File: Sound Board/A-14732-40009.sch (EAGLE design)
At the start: 197 parts, among them P2 AUX IN, P3 AUX OUT, P5 VOLUME, Q1 MPS3646, U1 OKI6295, U12 27C040-150, U13 27C040-150, U14 YAMAHA 2151, U15 TIL7524, U16 74LS374, U17 74LS174, U18 16L8, U19 74LS11, U2 2064, U20 74LS139, U21 74LS14, U22 74LS74, U23 74LS74, U26 74LS04, U28 YAMAHA 3012, U29 LM324D, U3 27C040, U30 MC3340, U31 HA3116, U32 TL084D, U33 TL084D, U4 6809E, U8 74LS138, U9 74LS74, Y1 3.5749MHz, Y2 8MHz

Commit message: 4th sheet added
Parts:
- added IC1: 74LS374DW, 74xx-us:74LS374DW
- added P1: (no value), SparkFun-Connectors:M10X2ROUND_NOSILK
- added P4: ORKIN R/W, SparkFun-Connectors:M04LONGPADS
- added U11, U24, U25: 26LS32A, A-14732-40009:26LS32A
- added U5, U6, U7: 26LS31, A-14732-40009:26LS31
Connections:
- net GND: now also P4.1
- net N$30: now also P4.4
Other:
- moved on the sheet: R4, U16P, U18, U19P, U20P, U21P, U22P, U23P, U26P, U8P, U9P

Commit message: wip
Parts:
- removed IC1: 74LS374DW, 74xx-us:74LS374DW
- added C27, C34, C35, C36, C37, C38, C39, C40, C41, C42, C43: 100pF, SparkFun-Capacitors:1.0UF50V10%(1206)
- added R12, R13, R14, R15, R16, R17, R18, R19, R20, R21, R47, R49, R50, R55, R56, R57, R58: 470, resistor:R-US_R1206
- added U10: 26LS32A, A-14732-40009:26LS32A
- U11, U24: value 26LS32A -> 26LS31; device A-14732-40009:26LS32A -> A-14732-40009:26LS31
- U5: value 26LS31 -> 74LS374DW; device A-14732-40009:26LS31 -> 74xx-us:74LS374DW
- U6: value 26LS31 -> 26LS32A; device A-14732-40009:26LS31 -> A-14732-40009:26LS32A
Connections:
- new net N$104: U5A.2Q, U7.INB
- new net N$105: U5A.3Q, U7.INC
- new net N$106: U5A.4Q, U7.IND
- new net N$107: U11.INA, U5A.5Q
- new net N$108: U11.INB, U5A.6Q
- new net N$109: U11.INC, U5A.7Q
- new net N$110: U11.IND, U5A.8Q
- new net N$111: U11.!EN, U7.!EN
- new net N$112: R58.1, U23B.D, U5A.OC
- new net N$98: U5A.1Q, U7.INA
- net 5V: now also U10.VCC, U11.VCC, U6.VCC, U7.VCC
- net ATE1: now also U23B.CLR, U9B.D, U9B.PRE
- net CPU0: now also U5A.1D, U6.OUTA
- net CPU1: now also U5A.2D, U6.OUTB
- net CPU2: now also U5A.3D, U6.OUTC
- net CPU3: now also U5A.4D, U6.OUTD
- net CPU4: now also U10.OUTA, U5A.5D
- net CPU5: now also U10.OUTB, U5A.6D
- net CPU6: now also U10.OUTC, U5A.7D
- net CPU7: now also U10.OUTD, U5A.8D
- net GND: now also R58.2, U10.EN, U10.GND, U11.EN, U11.GND, U6.GND, U7.EN, U7.GND
- net IRQ: now also U23B.Q
- net RD-LATCH: now also U10.!EN
- net WR-LATCH: now also U5A.CLK, U9B.CLK
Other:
- moved on the sheet: U11, U23B, U24, U6, U7, U9B

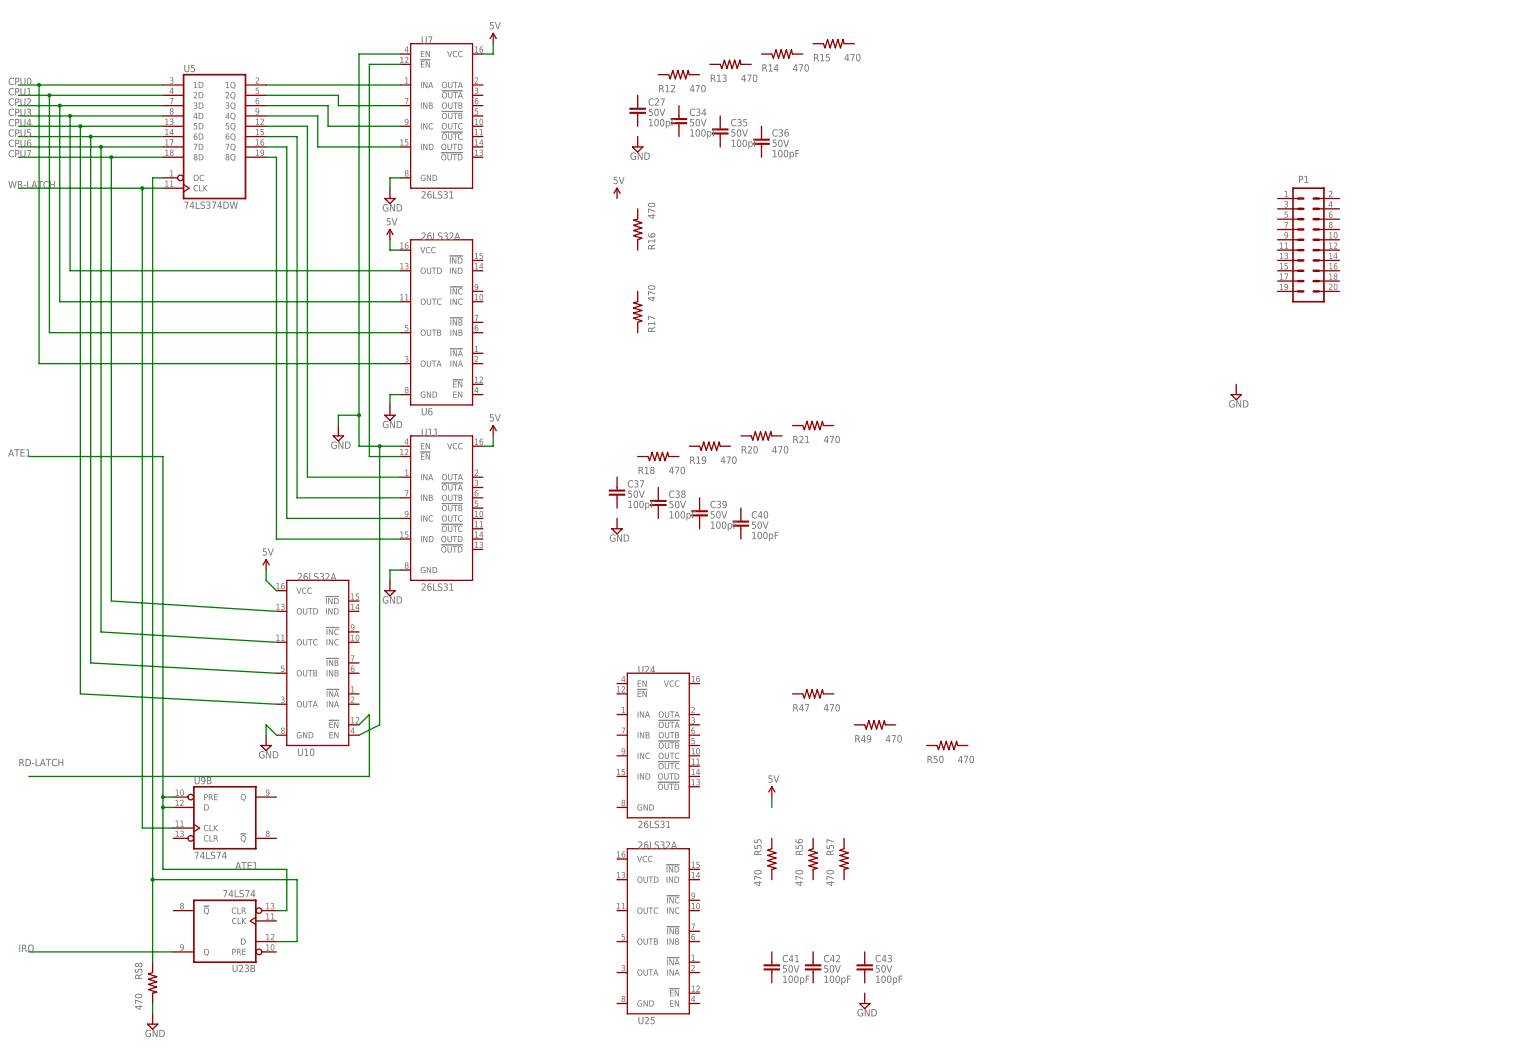
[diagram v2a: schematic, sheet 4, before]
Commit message: almost complete 4th sheet
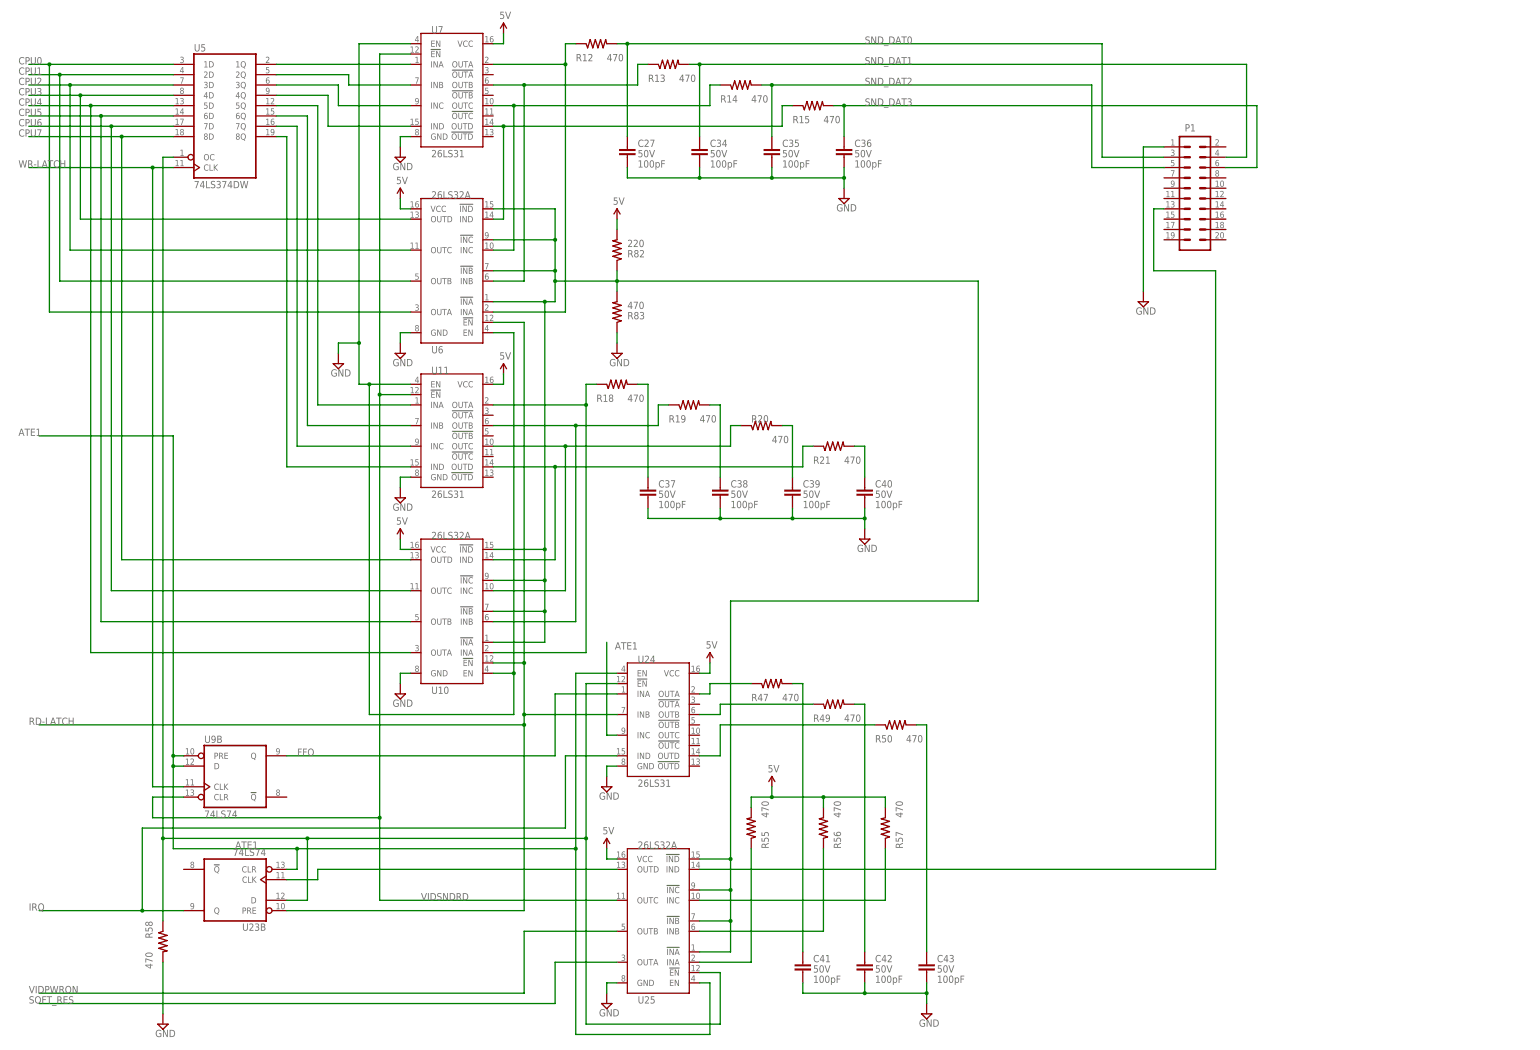
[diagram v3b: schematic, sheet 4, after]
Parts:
- removed R16, R17: 470, resistor:R-US_R1206
- added R82: 220, resistor:R-US_R1206
- added R83: 470, resistor:R-US_R1206
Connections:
- new net FFO: U24.INA, U9B.Q
- new net N$113: U23B.CLK, U25.OUTD
- new net N$114: R58.1, U23B.D, U24.!EN, U25.!EN, U5A.OC
- new net N$115: R12.1, U6.INA, U7.OUTA
- new net N$116: R19.1, U10.INB, U11.OUTB
- new net N$117: R13.1, U6.INB, U7.OUTB
- new net N$118: R20.1, U10.INC, U11.OUTC
- new net N$119: R21.1, U10.IND, U11.OUTD
- new net N$120: R82.1, R83.2, U10.!INA, U10.!INB, U10.!INC, U10.!IND, U25.!INA, U25.!INB, U25.!INC, U25.!IND, U6.!INA, U6.!INB, U6.!INC, U6.!IND
- new net N$121: C37.1, R18.2
- new net N$122: R14.1, U6.INC, U7.OUTC
- new net N$123: R15.1, U6.IND, U7.OUTD
- new net N$124: C38.1, R19.2
- new net N$125: C39.1, R20.2
- new net N$126: C40.1, R21.2
- new net N$127: R49.1, U24.OUTB
- new net N$128: R50.1, U24.OUTD
- new net N$129: C41.1, R47.2
- new net N$130: C42.1, R49.2
- new net N$131: C43.1, R50.2
- new net N$132: R55.1, U25.INA
- new net N$133: R56.1, U25.INB
- new net N$134: R57.1, U25.INC
- new net N$135: P1.13, U25.IND
- new net SND_DAT0: C27.1, P1.3, R12.2
- new net SND_DAT1: C34.1, P1.4, R13.2
- new net SND_DAT2: C35.1, P1.5, R14.2
- new net SND_DAT3: C36.1, P1.6, R15.2
- new net VIDSNDRD: U11.!EN, U25.OUTC, U7.!EN, U9B.CLR
- net 5V: now also R55.2, R56.2, R57.2, R82.2, U24.VCC, U25.VCC
- net ATE1: now also U24.EN, U24.INC, U25.EN
- net GND: now also C27.2, C34.2, C35.2, C36.2, C37.2, C38.2, C39.2, C40.2, C41.2, C42.2, C43.2, P1.1, R83.1, U24.GND, U25.GND, U6.EN
- net IRQ: now also U24.IND
- net N$111: now also R47.1, U24.OUTA; no longer U11.!EN, U7.!EN
- net N$112: now also R18.1, U10.INA, U11.OUTA; no longer R58.1, U23B.D, U5A.OC
- net RD-LATCH: now also U23B.PRE, U24.INB, U6.!EN
- net SOFT_RES: now also U25.OUTA
- net VIDPWRON: now also U25.OUTB
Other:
- moved on the sheet: C27, C34, C35, C36, C37, C38, C39, C40, C41, C42, C43, P1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

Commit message: P1 connected mostly wired up
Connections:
- net N$129: now also P1.19
- net N$130: now also P1.15
- net N$131: now also P1.11
- net N$132: now also P1.18
- net N$133: now also P1.17
- net N$134: now also P1.16
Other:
- moved on the sheet: C41, C42, C43, R55, R56, R57, U25

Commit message: completed 4th sheet, some parts name corrected
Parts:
- removed C27, C34: 100pF, SparkFun-Capacitors:1.0UF50V10%(1206)
- removed R47, R49, R50, R58: 470, resistor:R-US_R1206
- added C44, C45: 100pF, SparkFun-Capacitors:1.0UF50V10%(1206)
- added R16, R17: 47, resistor:R-US_R1206
- added R84, R91: 4.7K, resistor:R-US_R1206
- R11: value 100K -> 47
- R12, R13, R14, R15, R18, R19, R20, R21: value 470 -> 47
- R4: value 4.7K -> 100
- R55: value 470 -> 100K
- R85, R86: value 470 -> 4.7K
- renumbered R56 to R85, R57 to R86
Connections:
- net N$133 renamed B_VIDRES
- net N$135 renamed B_VIDDAV
- removed net CPU0: U1.D0, U14.D0, U15.D0, U17A.D2, U5A.1D, U6.OUTA
- removed net CPU1: U1.D1, U14.D1, U15.D1, U17A.D6, U5A.2D, U6.OUTB
- removed net CPU2: U1.D2, U14.D2, U15.D2, U17A.D3, U5A.3D, U6.OUTC
- removed net CPU3: U1.D3, U14.D3, U15.D3, U5A.4D, U6.OUTD
- removed net CPU4: U1.D4, U10.OUTA, U14.D4, U15.D4, U5A.5D
- removed net CPU5: U1.D5, U10.OUTB, U14.D5, U15.D5, U5A.6D
- removed net CPU6: U1.D6, U10.OUTC, U14.D6, U15.D6, U5A.7D
- removed net CPU7: U1.D7, U10.OUTD, U14.D7, U15.D7, U5A.8D
- removed net N$121: C37.1, R18.2
- removed net N$124: C38.1, R19.2
- removed net N$125: C39.1, R20.2
- removed net N$126: C40.1, R21.2
- removed net N$129: C41.1, P1.19, R47.2
- removed net N$130: C42.1, P1.15, R49.2
- removed net N$131: C43.1, P1.11, R50.2
- removed net N$132: P1.18, R55.1, U25.INA
- new net B_SND_RD: C44.1, P1.15, R20.2
- new net SND_DAT4: C39.1, P1.7, R15.2
- new net SND_DAT5: C40.1, P1.8, R16.2
- new net SND_DAT6: C41.1, P1.9, R17.2
- new net SND_DAT7: C42.1, P1.10, R18.2
- new net SND_DAT8: P1.18, R84.1, U25.INA
- new net SND_DAV: C45.1, P1.19, R21.2
- new net SND_RDY: C43.1, P1.11, R19.2
- net +12VDEC: now also R55.2; no longer R11.2
- net 5V: now also R84.2, R91.2; no longer R4.2, R55.2
- net D0: now also U1.D0, U14.D0, U15.D0, U17A.D2, U5A.1D, U6.OUTA
- net D1: now also U1.D1, U14.D1, U15.D1, U17A.D6, U5A.2D, U6.OUTB
- net D2: now also U1.D2, U14.D2, U15.D2, U17A.D3, U5A.3D, U6.OUTC
- net D3: now also U1.D3, U14.D3, U15.D3, U5A.4D, U6.OUTD
- net D4: now also U1.D4, U10.OUTA, U14.D4, U15.D4, U5A.5D
- net D5: now also U1.D5, U10.OUTB, U14.D5, U15.D5, U5A.6D
- net D6: now also U1.D6, U10.OUTC, U14.D6, U15.D6, U5A.7D
- net D7: now also U1.D7, U10.OUTD, U14.D7, U15.D7, U5A.8D
- net GND: now also C44.2, C45.2, R4.2; no longer C27.2, C34.2, R58.2
- net N$111: now also R21.1; no longer R47.1
- net N$112: now also R15.1; no longer R18.1
- net N$114: now also R4.1; no longer R58.1
- net N$115: now also R11.1; no longer R12.1
- net N$116: now also R16.1; no longer R19.1
- net N$118: now also R17.1; no longer R20.1
- net N$119: now also R18.1; no longer R21.1
- net N$123: now also R12.1; no longer R15.1
- net N$127: now also R20.1; no longer R49.1
- net N$128: now also R19.1; no longer R50.1
- net N$30: now also R91.1; no longer R4.1
- net N$60: now also R55.1; no longer R11.1
- net SND_DAT0: now also C35.1, R11.2; no longer C27.1, R12.2
- net SND_DAT1: now also C37.1; no longer C34.1
- net SND_DAT2: now also C38.1; no longer C35.1
- net SND_DAT3: now also R12.2; no longer R15.2
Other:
- note added: "CPU BUS"
- moved on the sheet: C35, C37, C38, C39, C40, C41, C42, P1, P4, R12, R15, R18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

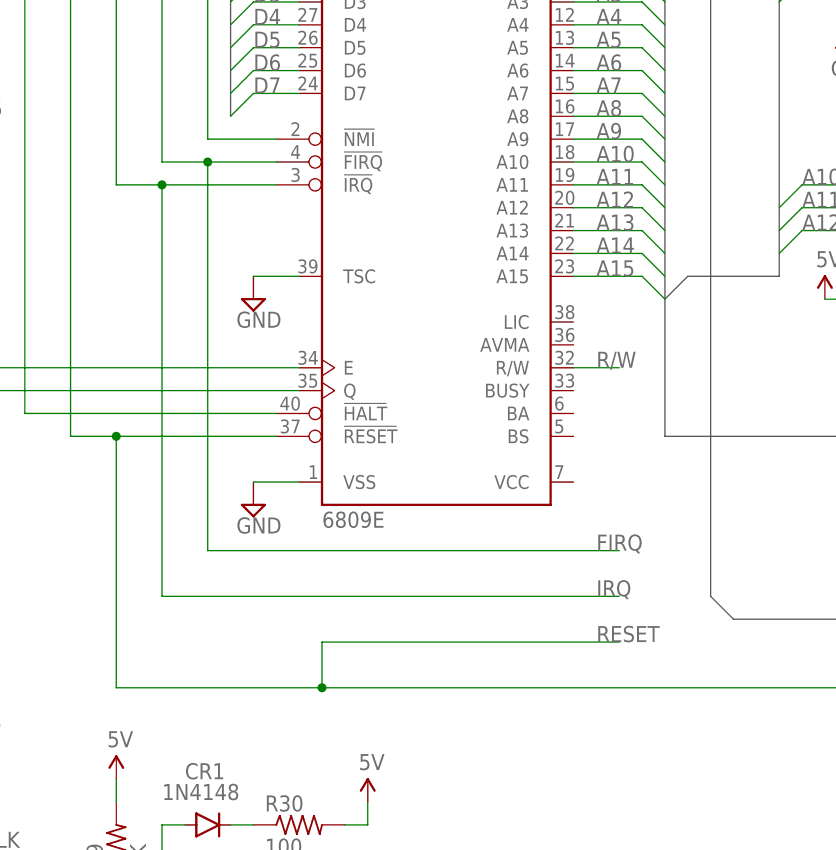
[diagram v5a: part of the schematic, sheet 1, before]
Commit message: fixed YAM-OUT2 net connection, fixed mixed up GND<->AGND, fixed missed power supply pins for U5
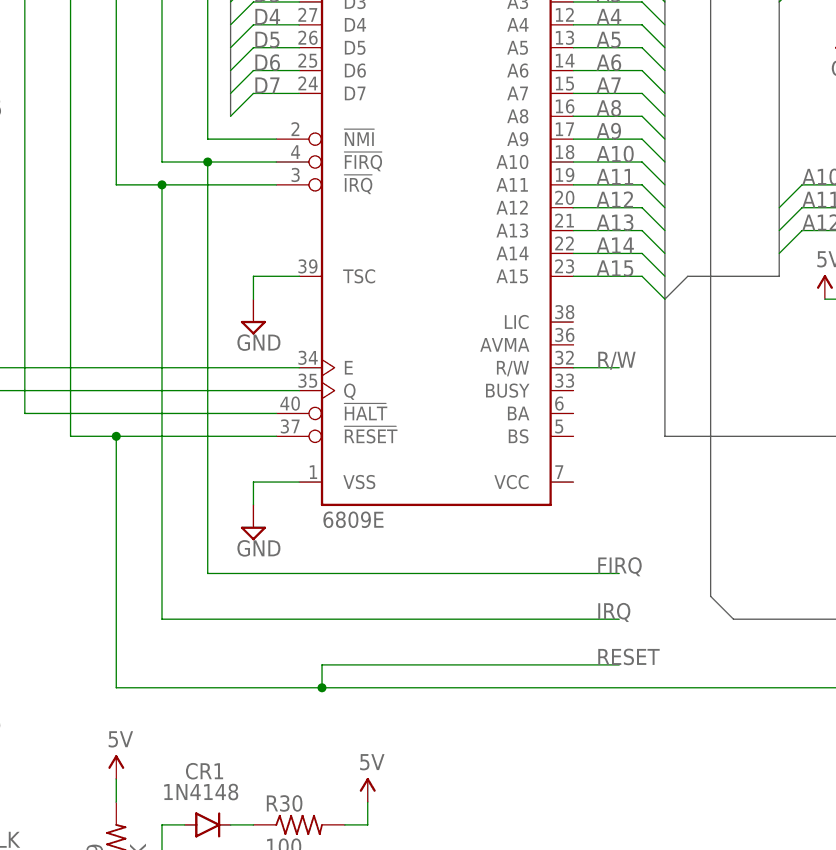
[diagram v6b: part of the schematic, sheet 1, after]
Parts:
- P6, P7: value (none) -> 0.156"
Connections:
- net 5V: now also U5P.VCC
- net AGND: no longer C3.2, C6.2, C7.2, MTG1.P$1, MTG2.P$1, MTG3.P$1, MTG4.P$1, Q1.E, U4.TSC
- net GND: now also C3.2, C6.2, C7.2, MTG1.P$1, MTG2.P$1, MTG3.P$1, MTG4.P$1, Q1.E, U4.TSC, U5P.GND
- net YAM1-OUT: no longer R44.2
- net YAM2-OUT: now also R44.2
